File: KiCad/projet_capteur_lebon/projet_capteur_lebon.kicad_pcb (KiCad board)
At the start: 2 copper layers, 68.6 x 53.3 mm, 22 parts, among them J1 Power, J2 Digital/PWM, J3 Analog, J4 Digital/PWM

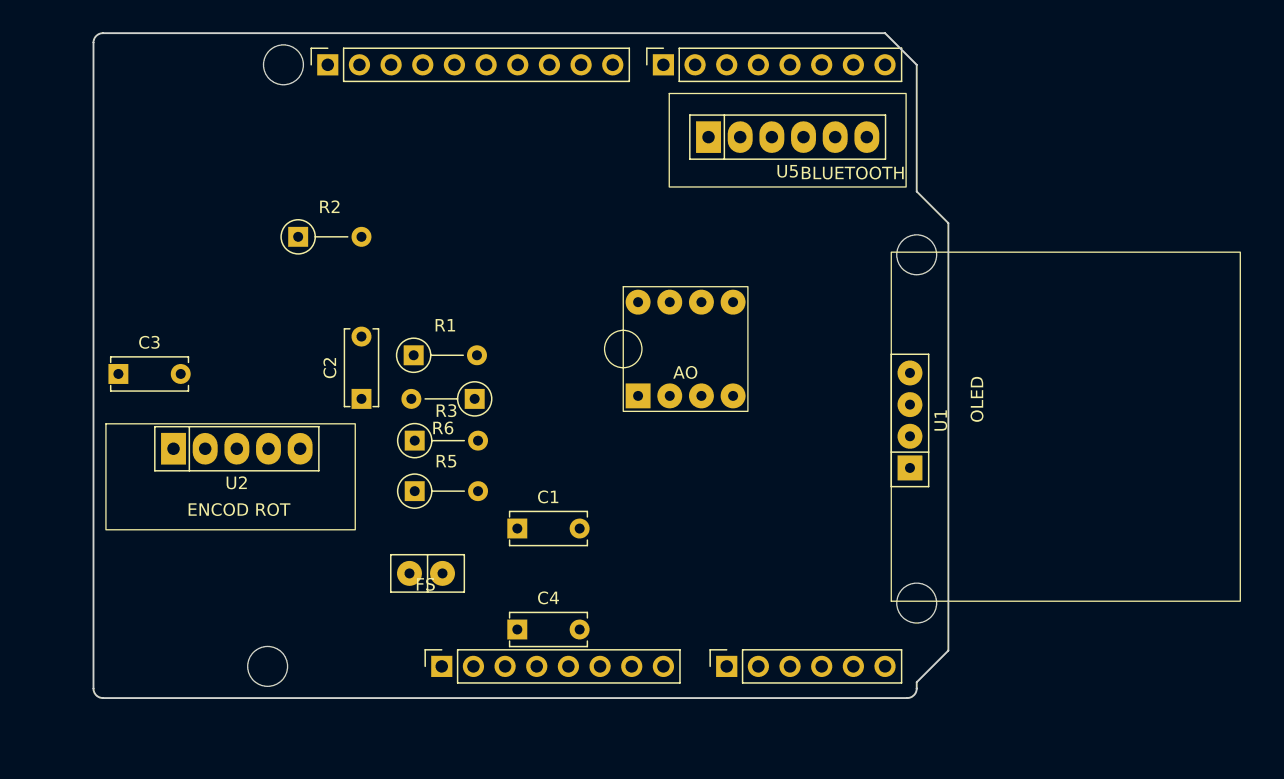
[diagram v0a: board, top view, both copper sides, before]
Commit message: etiquettes + digital pot
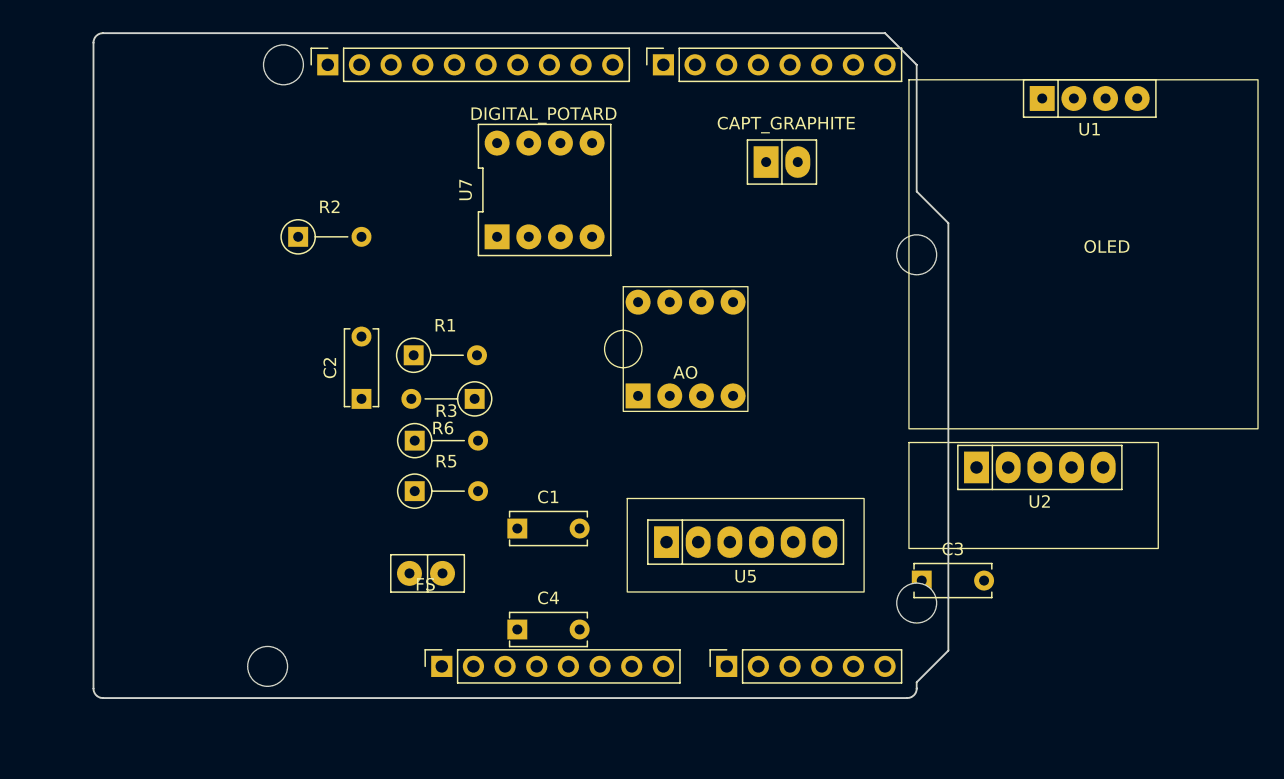
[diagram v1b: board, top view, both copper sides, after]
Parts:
- added U7: ~, librairie_empreintes:DIP-8_296, F.Cu at (136.2, 59.2)
- added U8: ~, librairie_empreintes:CAPTEUR_GRAPHITE, F.Cu at (156.0, 63.0)
- moved C3 66.5 mm to (166.4, 90.6)
- moved U2 64.4 mm to (175.9, 81.5)
- moved U5 32.7 mm to (152.3, 87.5)
- moved U1 29.6 mm to (179.9, 51.9), turned to 0 degrees
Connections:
- net Net-(U4-IN-) renamed R2

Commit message: fin schématique liaisons etc reste debug U5
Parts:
- added U6: ~, librairie_empreintes:SIP-3, F.Cu at (156.5, 63.5)
- added U9: ~, librairie_empreintes:BLUETOOTH, F.Cu at (154.7, 83.0)
- U5: footprint librairie_empreintes:BLUETOOTH -> librairie_empreintes:SIP-2
- moved U2 66.6 mm to (110.7, 68.3)
- moved U5 5.10 mm to (148.1, 90.4)
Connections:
- C2 pad 1: output -> CAPT_AMPL
- C3 pad 1: EROT 1 -> CLK
- J1 pad 5: +5V -> 5V
- J2 pad 1: /SCL/A5 -> SCL
- J2 pad 10: /8 -> TXD
- J2 pad 2: /SDA/A4 -> SDA
- J2 pad 3: /AREF -> /13
- J3 pad 1: /A0 -> CAPT_AMPL
- J3 pad 2: /A1 -> OUT_FLEX
- J3 pad 5: /SDA/A4 -> SDA
- J3 pad 6: /SCL/A5 -> SCL
- J4 pad 1: /7 -> RX
- J4 pad 2: /*6 -> SW
- J4 pad 4: /4 -> DT
- J4 pad 6: /2 -> CLK
- R2 pad 1: Analog voltage -> OUT_FLEX
- R5 pad 1: unconnected-(R5-Pad1) -> OUT_CAPT
- R6 pad 2: output -> CAPT_AMPL
- U1 pad 3: OLED 3 -> SCL
- U1 pad 4: OLED 4 -> SDA
- U2 pad 1: EROT 1 -> CLK
- U2 pad 2: EROT 2 -> DT
- U2 pad 3: EROT 3 -> SW
- U7 pad 1: /8 -> /*10

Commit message: modeles 3d et routage
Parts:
- removed U3: ~, librairie_empreintes:SIP-2
- moved C4 41.4 mm to (103.5, 66.5)
- moved R4 39.5 mm to (142.2, 93.0)
- moved U2 37.5 mm to (145.5, 54.5), turned to 180 degrees
- moved C3 35.2 mm to (157.5, 56.5)
- moved U8 30.5 mm to (126.0, 68.5), turned to -90 degrees
- moved U1 30.2 mm to (166.5, 79.0), turned to -90 degrees
- moved U9 29.2 mm to (125.8, 87.5)
- moved U6 28.7 mm to (128.0, 60.0)
- moved R3 28.5 mm to (103.2, 62.0)
- moved C1 26.0 mm to (110.0, 76.5)
- moved U4 24.4 mm to (123.2, 74.3)
- moved U7 20.2 mm to (116.0, 59.5), turned to 180 degrees
- moved R1 17.7 mm to (110.2, 81.0)
- moved R6 17.5 mm to (113.8, 71.0)
- moved C2 16.4 mm to (105.5, 79.5)
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- renumbered R2 to R4
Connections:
- J2 pad 3: /13 -> /AREF
- U4 pad 7: +5V -> 5V
- U5 pad 1: (no net) -> 5V
- U5 pad 2: (no net) -> OUT_FLEX
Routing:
- net 5V: track 0.00 -> 187.7 mm
- net GND: track 0.00 -> 87.8 mm, vias 0 -> 9
- net CAPT_AMPL: track 0.00 -> 74.3 mm, vias 0 -> 2
- net R2: track 0.00 -> 56.4 mm
- net RX: track 0.00 -> 47.3 mm
- net TXD: track 0.00 -> 45.1 mm
- net Net-(U4-IN+): track 0.00 -> 36.3 mm
- net /*11: track 0.00 -> 29.7 mm
- net Net-(U4-OUT): track 0.00 -> 24.3 mm
- net OUT_FLEX: track 0.00 -> 22.5 mm
- net SDA: track 0.00 -> 22.2 mm
- net /*10: track 0.00 -> 21.0 mm
- net SCL: track 0.00 -> 18.4 mm
- net /*9: track 0.00 -> 18.3 mm
- net CLK: track 0.00 -> 15.4 mm
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- added copper zone on B.Cu, net GND

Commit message: finitions pcb et gerber
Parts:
- moved U5 2.75 mm to (131.2, 93.8)
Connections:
- U7 pad 5: R2 -> GND
- U7 pad 7: GND -> R2
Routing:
- net GND: track 87.8 -> 56.9 mm, vias 9 -> 12
- net R2: track 56.4 -> 68.6 mm
- net OUT_FLEX: track 22.5 -> 25.3 mm
- net CAPT_AMPL: track 74.3 -> 73.2 mm, vias 2 -> 0
- net /13: track 15.2 -> 16.2 mm
